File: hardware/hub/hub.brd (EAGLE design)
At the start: 45.7 x 44.1 mm, 22 parts, among them IC1 7805TV, IC2 LM3940, J1 AVR_SPI_PRG_6PTH, J2 POWER_JACKPTH, U1 ATMEGA328P_PDIP, U2 ENC28J60, U3 NRF24L01+

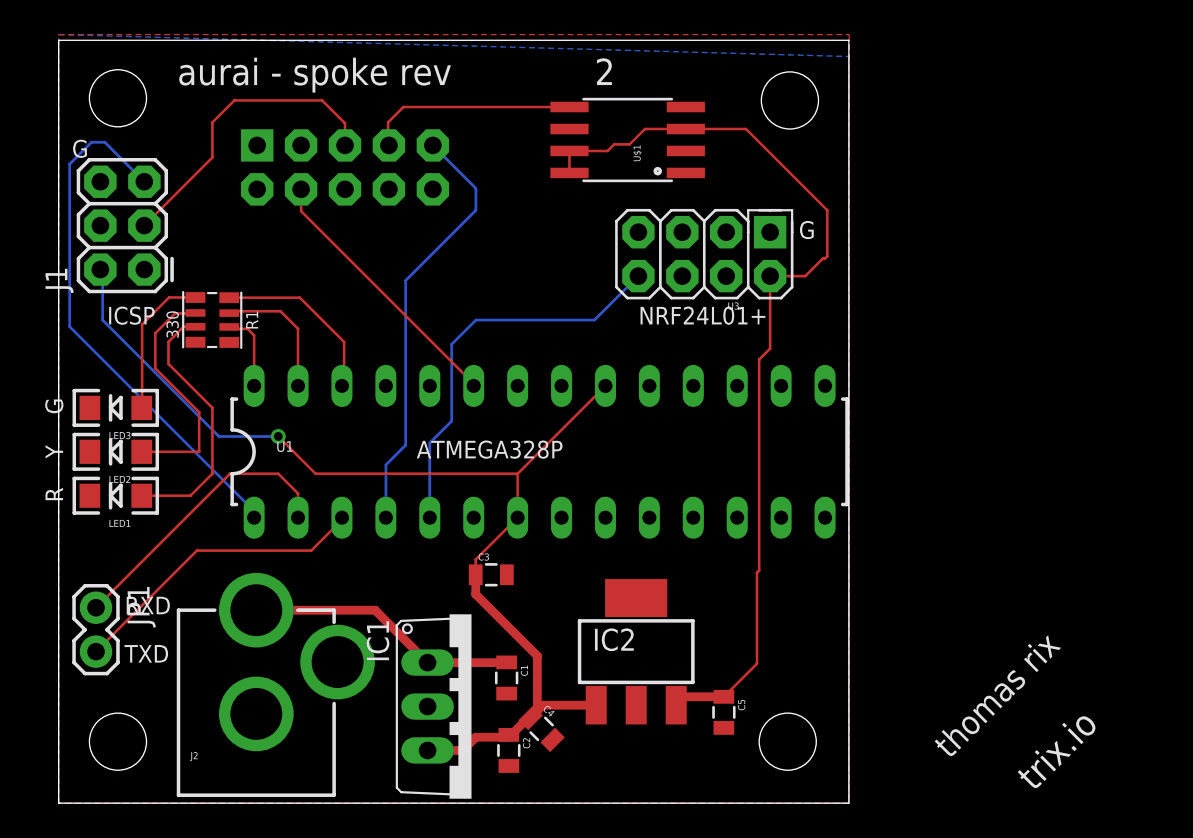
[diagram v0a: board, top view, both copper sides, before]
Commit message: Fix flash pinout. Finish hub brd
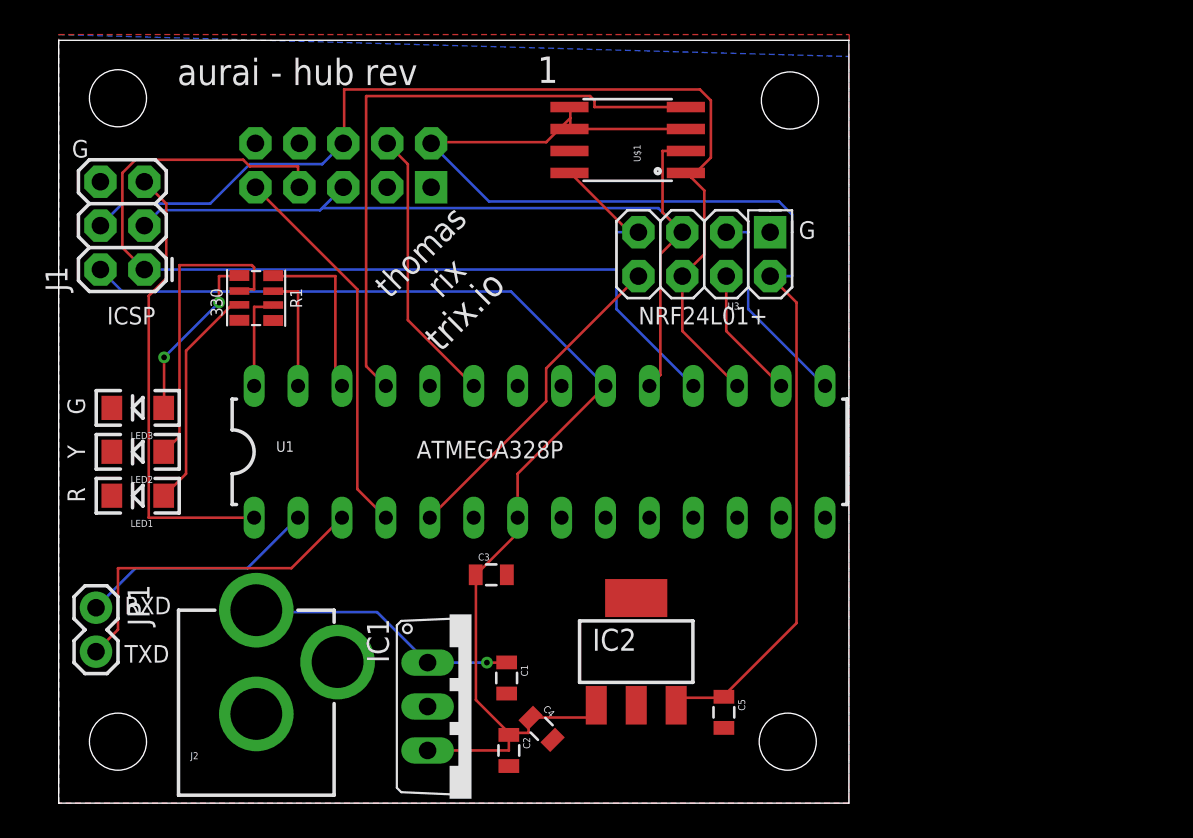
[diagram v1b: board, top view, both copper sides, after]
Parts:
- moved R1 2.84 mm to (11.4, 29.2)
- moved LED1 1.27 mm to (4.57, 17.8)
- moved LED2 1.27 mm to (4.57, 20.3)
- moved LED3 1.27 mm to (4.57, 22.9)
- turned U2 to 90 degrees
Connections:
- net 3.3V: now also U$1.5, U$1.6; no longer U$1.7, U$1.8
- net GND: now also U$1.7; no longer U$1.6
- net MISO: now also U$1.8; no longer U$1.5
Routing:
- net MOSI: track 0.00 -> 60.6 mm
- net MISO: track 12.6 -> 62.7 mm
- net N$11: track 0.13 -> 36.2 mm
- net SCK: track 17.6 -> 50.0 mm
- net 3.3V: track 53.6 -> 74.0 mm
- net N$7: track 0.00 -> 12.0 mm
- net N$9: track 0.00 -> 7.67 mm
- net RESET: track 30.7 -> 26.5 mm
- net N$10: track 23.0 -> 19.0 mm
- net N$8: track 14.0 -> 17.7 mm
- net N$2: track 16.8 -> 13.8 mm
- net 5V: track 65.5 -> 68.2 mm, vias 1 -> 0
- net N$15: track 24.7 -> 22.2 mm
- net N$1: track 15.2 -> 13.2 mm
- net N$4: track 17.5 -> 19.5 mm
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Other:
- board text added: "aurai - hub rev"
- board text removed: "aurai - spoke rev"
